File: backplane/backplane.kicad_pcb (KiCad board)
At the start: 2 copper layers, 150 x 150 mm, 16 parts

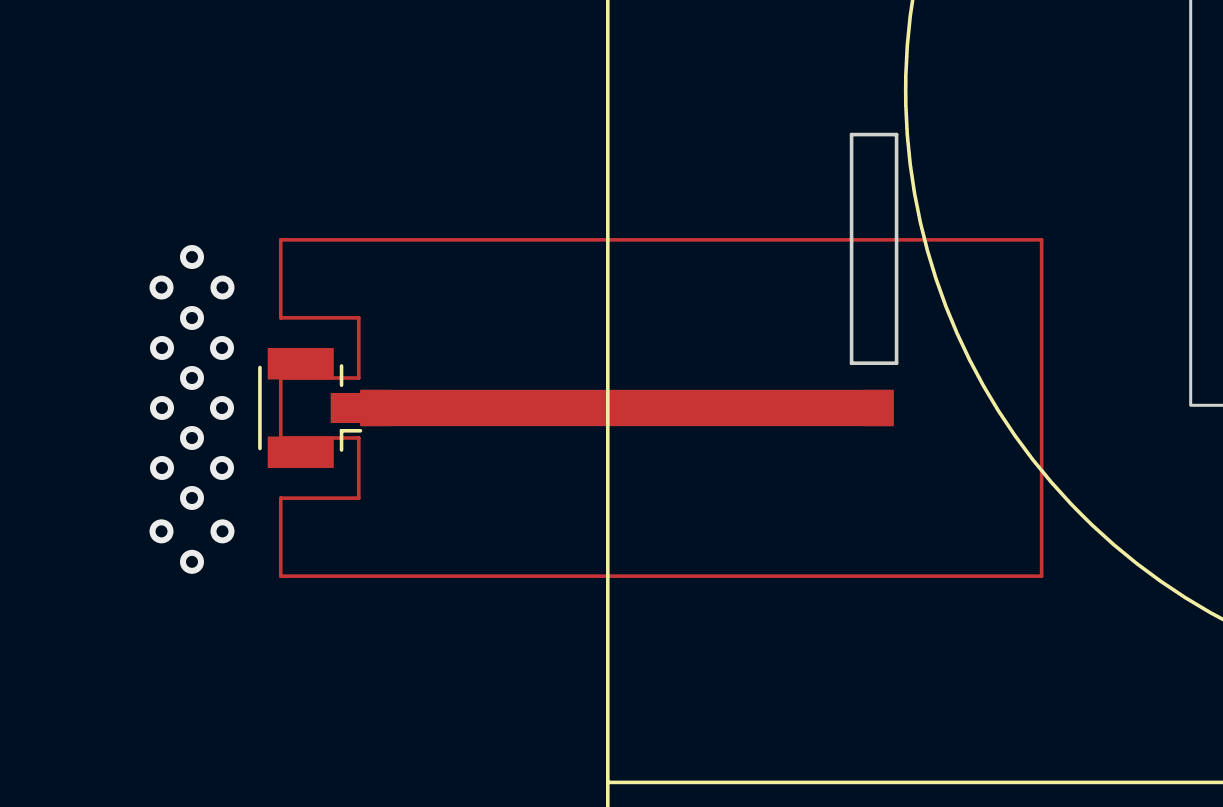
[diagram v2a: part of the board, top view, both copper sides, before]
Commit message: Replaced transformer isolation with "Keep Out" zones
Was previously using a copper trace to isolate the transformer to prevent
copper fill to get around it.  Found keep out zone option to define areas
that we don't want copper to be in.
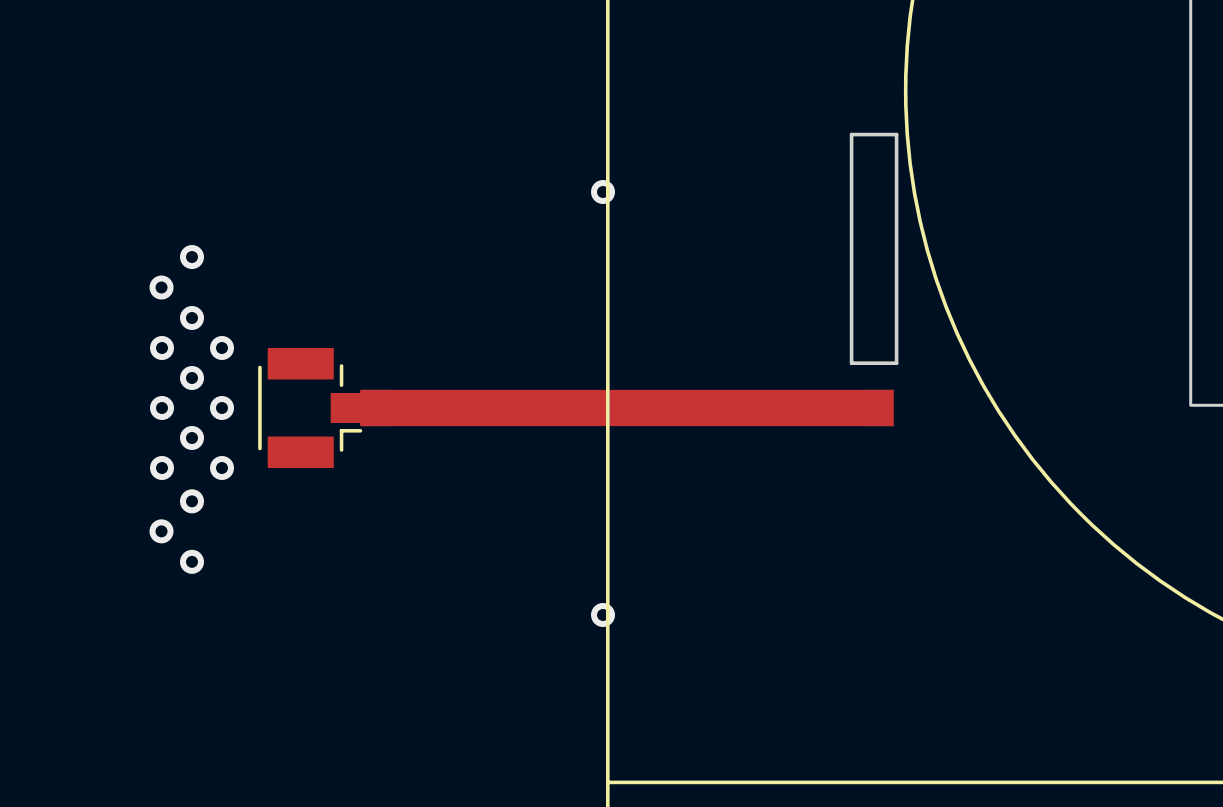
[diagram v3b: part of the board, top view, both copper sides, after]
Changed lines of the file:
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@@
   (module muwave_stub locked (layer F.Cu)
     (at 62.03385 116 270)
-    (fp_text reference REF** (at -1.27 0.5 90) (layer B.Fab) hide
+    (fp_text reference REF** (at -1.27 0.5 270) (layer B.Fab) hide
       (effects (font (size 0.25 0.25) (thickness 0.05)))
     )
-    (fp_text value muwave_stub (at 0 -0.5 90) (layer F.Fab)
+    (fp_text value muwave_stub (at 0 -0.5 270) (layer F.Fab)
       (effects (font (size 0.25 0.25) (thickness 0.05)))
     )
-    (fp_line (start -3.00469 2.475001) (end -3.00469 5.075001) (layer F.Cu) (width 0.12))
-    (fp_line (start 1 2.475001) (end 1 5.075001) (layer F.Cu) (width 0.12))
-    (fp_line (start -1 5.075001) (end 1 5.075001) (layer F.Cu) (width 0.12))
-    (fp_line (start -5.60469 5.075001) (end -3.00469 5.075001) (layer F.Cu) (width 0.12))
-    (fp_line (start -5.60469 -20.287299) (end 5.60469 -20.287299) (layer F.Cu) (width 0.12))
-    (fp_line (start -5.60469 -20.287299) (end -5.60469 5.075001) (layer F.Cu) (width 0.12))
-    (fp_line (start -1 2.475001) (end -1 5.075001) (layer F.Cu) (width 0.12))
-    (fp_line (start -3.00469 2.475001) (end -1 2.475001) (layer F.Cu) (width 0.12))
-    (fp_line (start 3.00469 2.475001) (end 1 2.475001) (layer F.Cu) (width 0.12))
-    (fp_line (start 5.60469 -20.287299) (end 5.60469 5.075001) (layer F.Cu) (width 0.12))
-    (fp_line (start 5.60469 5.075001) (end 3.00469 5.075001) (layer F.Cu) (width 0.12))
-    (fp_line (start 3.00469 2.475001) (end 3.00469 5.075001) (layer F.Cu) (width 0.12))
     (pad 1 smd rect (at 0 -6.46615 270) (size 1.20938 17.7623) (layers F.Cu))
     (pad 1 smd rect (at 0 -14.8473 270) (size 1.20938 1) (layers F.Cu F.Mask))
@@
   (gr_line (start 172.86 30.48) (end 172.86 180.48) (layer Edge.Cuts) (width 0.05))
   (gr_line (start 22.86 30.48) (end 172.86 30.48) (layer Edge.Cuts) (width 0.05))
+  (via (at 67.7 108.8) (size 0.8) (drill 0.4) (layers F.Cu B.Cu) (net 1))
+  (via (at 67.7 122.9) (size 0.8) (drill 0.4) (layers F.Cu B.Cu) (net 1))
   (via (at 52.984 111.984) (size 0.8) (drill 0.4) (layers F.Cu B.Cu) (net 1))
-  (via (at 55.016 111.984) (size 0.8) (drill 0.4) (layers F.Cu B.Cu) (net 1))
   (via (at 54 110.968) (size 0.8) (drill 0.4) (layers F.Cu B.Cu) (net 1))
-  (via (at 55.016 120.112) (size 0.8) (drill 0.4) (layers F.Cu B.Cu) (net 1))
   (via (at 52.984 120.112) (size 0.8) (drill 0.4) (layers F.Cu B.Cu) (net 1))
   (via (at 54 121.128) (size 0.8) (drill 0.4) (layers F.Cu B.Cu) (net 1))
@@
   (via (at 54 117) (size 0.8) (drill 0.4) (layers F.Cu B.Cu) (net 1))
   (via (at 55 118) (size 0.8) (drill 0.4) (layers F.Cu B.Cu) (net 1))
-  (via (at 54 119) (size 0.8) (drill 0.4) (layers F.Cu B.Cu) (net 1))
+  (via (at 54 119.112) (size 0.8) (drill 0.4) (layers F.Cu B.Cu) (net 1))
   (via (at 53 114) (size 0.8) (drill 0.4) (layers F.Cu B.Cu) (net 1))
   (via (at 53 116) (size 0.8) (drill 0.4) (layers F.Cu B.Cu) (net 1))
@@
       )
     )
+  )
+  (zone (net 0) (net_name "") (layer F.Cu) (hatch full 0.508)
+    (connect_pads (clearance 0.508))
+    (min_thickness 0.254)
+    (keepout (tracks not_allowed) (vias not_allowed) (copperpour not_allowed))
+    (fill (arc_segments 32) (thermal_gap 0.508) (thermal_bridge_width 0.508))
+    (polygon
+      (pts
+        (xy 56.896 110.236) (xy 56.896 121.92) (xy 82.4 121.92) (xy 82.4 110.236)
+      )
+    )
+  )
+  (zone (net 0) (net_name "") (layer F.Cu) (hatch full 0.508)
+    (connect_pads (clearance 0.508))
+    (min_thickness 0.254)
+    (keepout (tracks not_allowed) (vias not_allowed) (copperpour not_allowed))
+    (fill (arc_segments 32) (thermal_gap 0.508) (thermal_bridge_width 0.508))
+    (polygon
+      (pts
+        (xy 58.547 115.062) (xy 58.547 116.967) (xy 56.007 116.967) (xy 56.007 115.062)
+      )
+    )
+  )
+  (zone (net 0) (net_name "") (layer F.Cu) (hatch full 0.508)
+    (connect_pads (clearance 0.508))
+    (min_thickness 0.254)
+    (keepout (tracks not_allowed) (vias not_allowed) (copperpour not_allowed))
+    (fill (arc_segments 32) (thermal_gap 0.508) (thermal_bridge_width 0.508))
+    (polygon
+      (pts
+        (xy 59.6 113.5) (xy 59.6 110.2) (xy 54.6 110.2) (xy 54.6 113.5)
+      )
+    )
+  )
+  (zone (net 0) (net_name "") (layer F.Cu) (hatch full 0.508)
+    (connect_pads (clearance 0.508))
+    (min_thickness 0.254)
+    (keepout (tracks not_allowed) (vias not_allowed) (copperpour not_allowed))
+    (fill (arc_segments 32) (thermal_gap 0.508) (thermal_bridge_width 0.508))
+    (polygon
+      (pts
+        (xy 59.569677 121.9) (xy 59.569677 118.6) (xy 54.569677 118.6) (xy 54.569677 121.9)
+      )
+    )

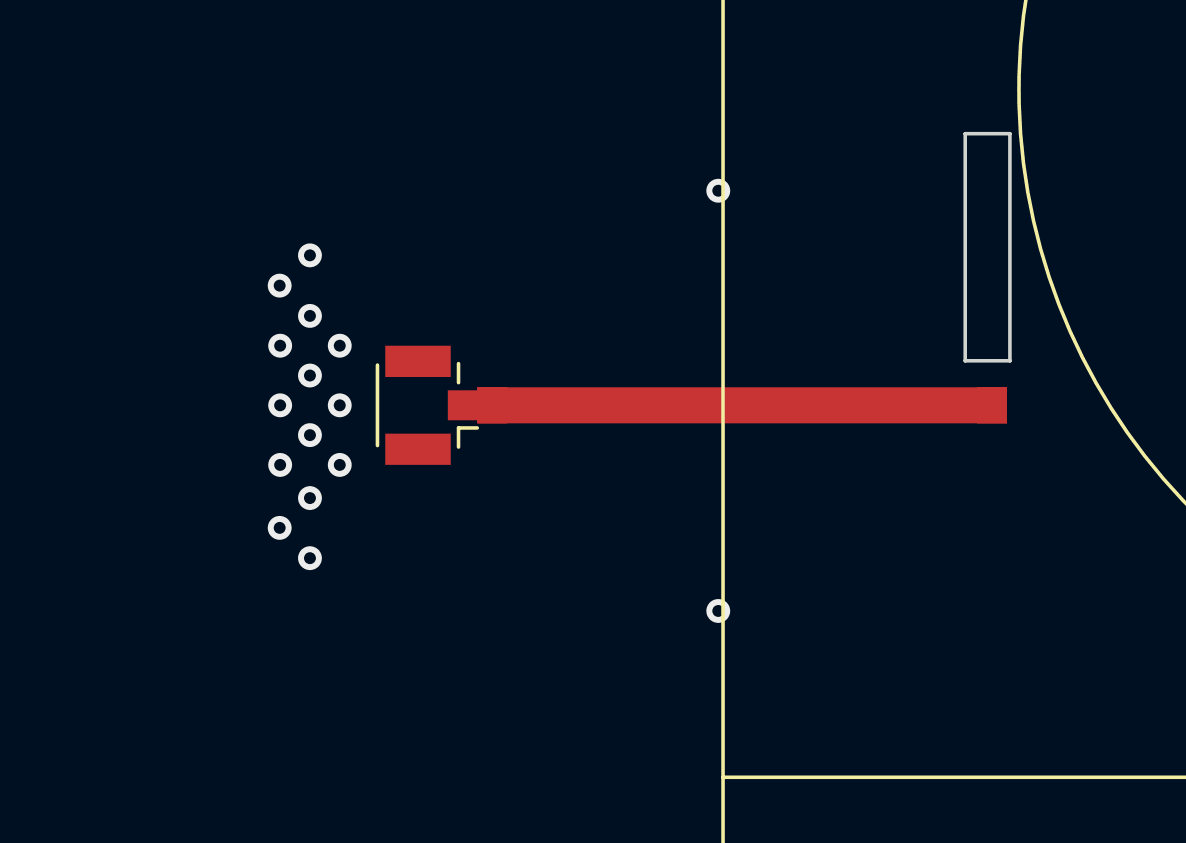
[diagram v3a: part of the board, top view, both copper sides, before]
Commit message: Updating to experimental version of backplane
Transformer strip is now 2mm wider
Added gap between U.FL connector and microstrip for capacitor in series
Microstrip has a tapered tab for capacitor
Added gerber to apply via holes for ONLY around the U.FL connector
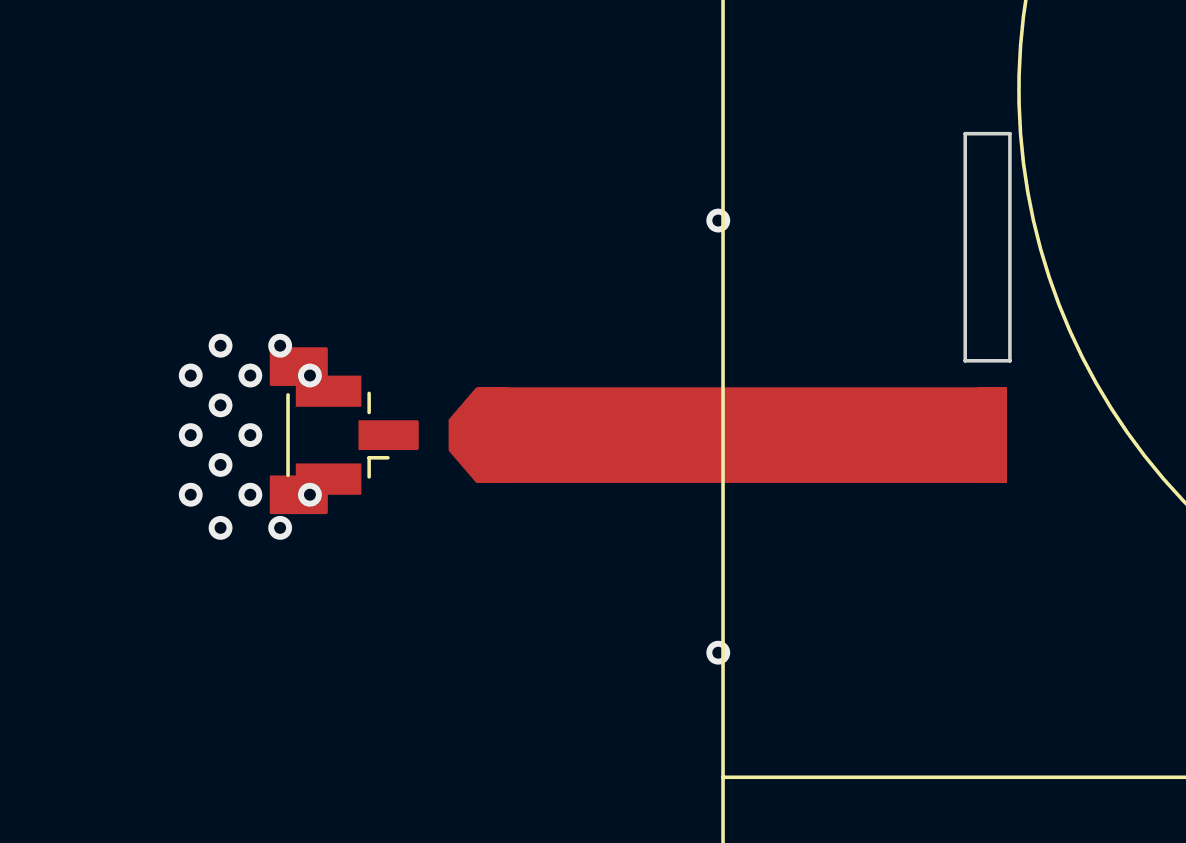
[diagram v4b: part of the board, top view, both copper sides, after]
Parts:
- moved REF** 3.16 mm to (55.1, 117.0)
- moved REF** 1.00 mm to (62.0, 117.0)
